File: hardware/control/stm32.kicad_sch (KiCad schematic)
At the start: 18 parts, among them U201 STM32L431RCTx

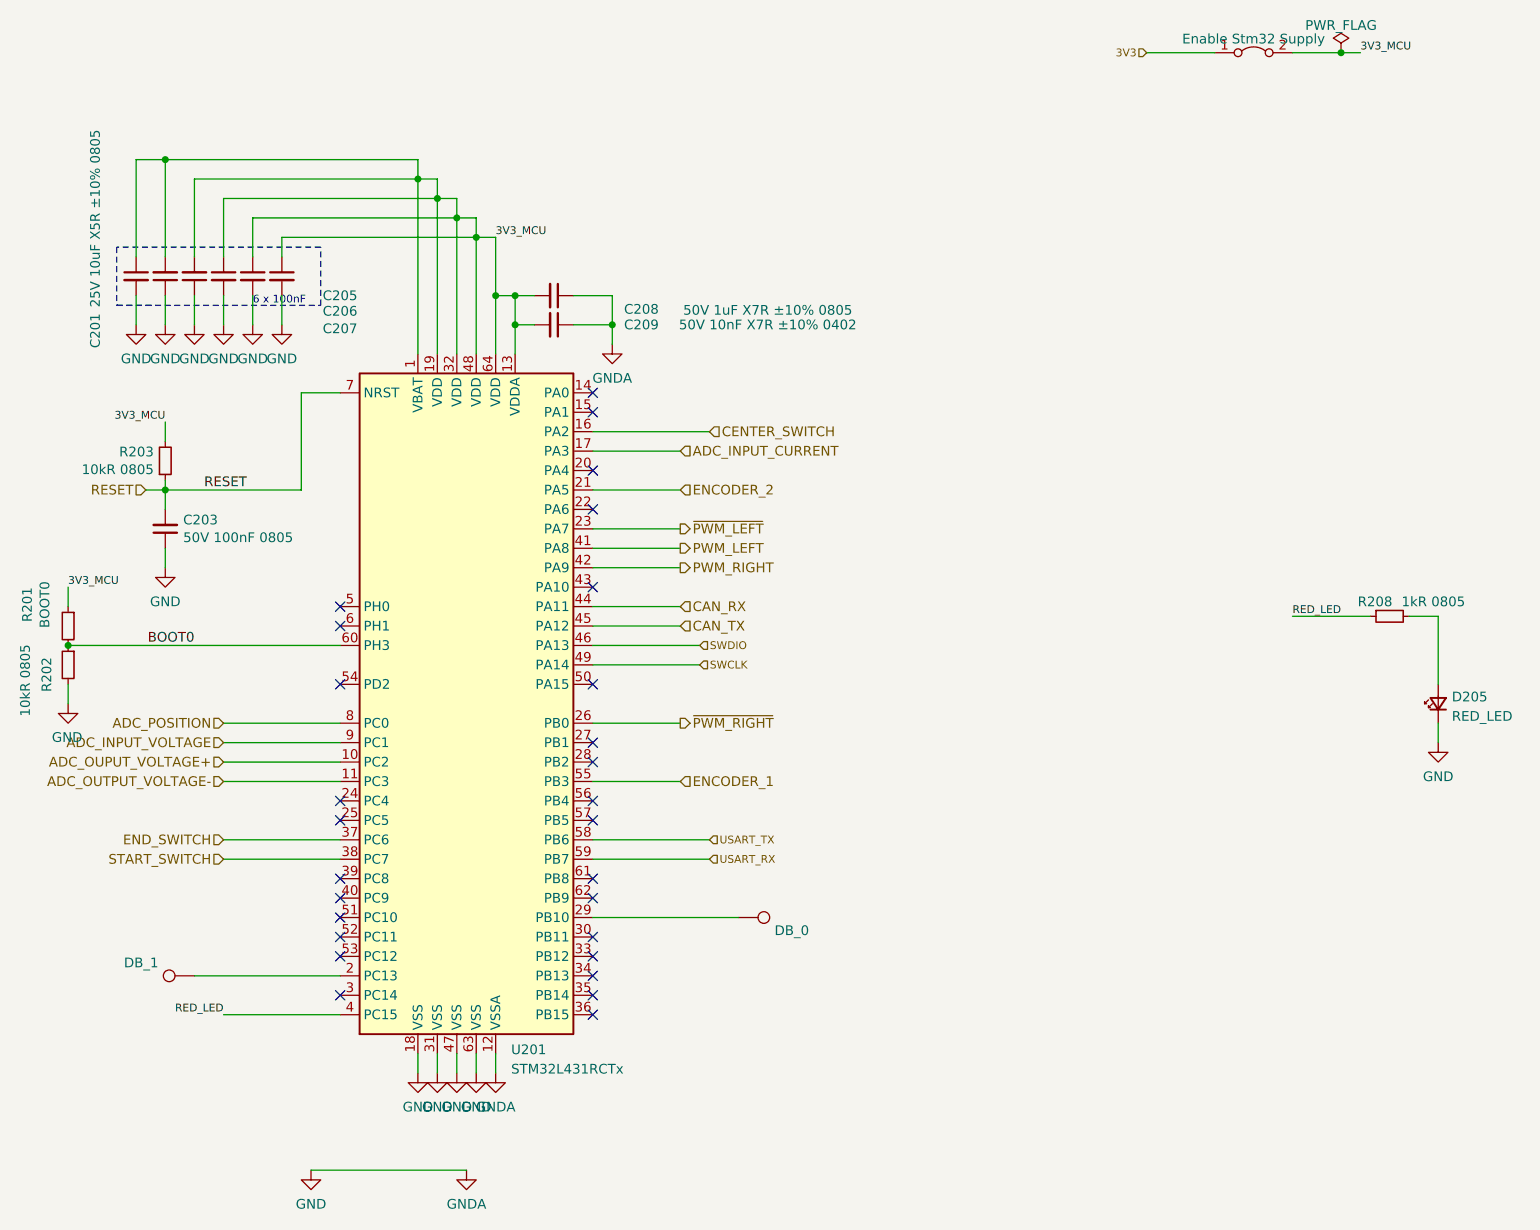
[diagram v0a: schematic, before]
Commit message: Organize schematics per domain
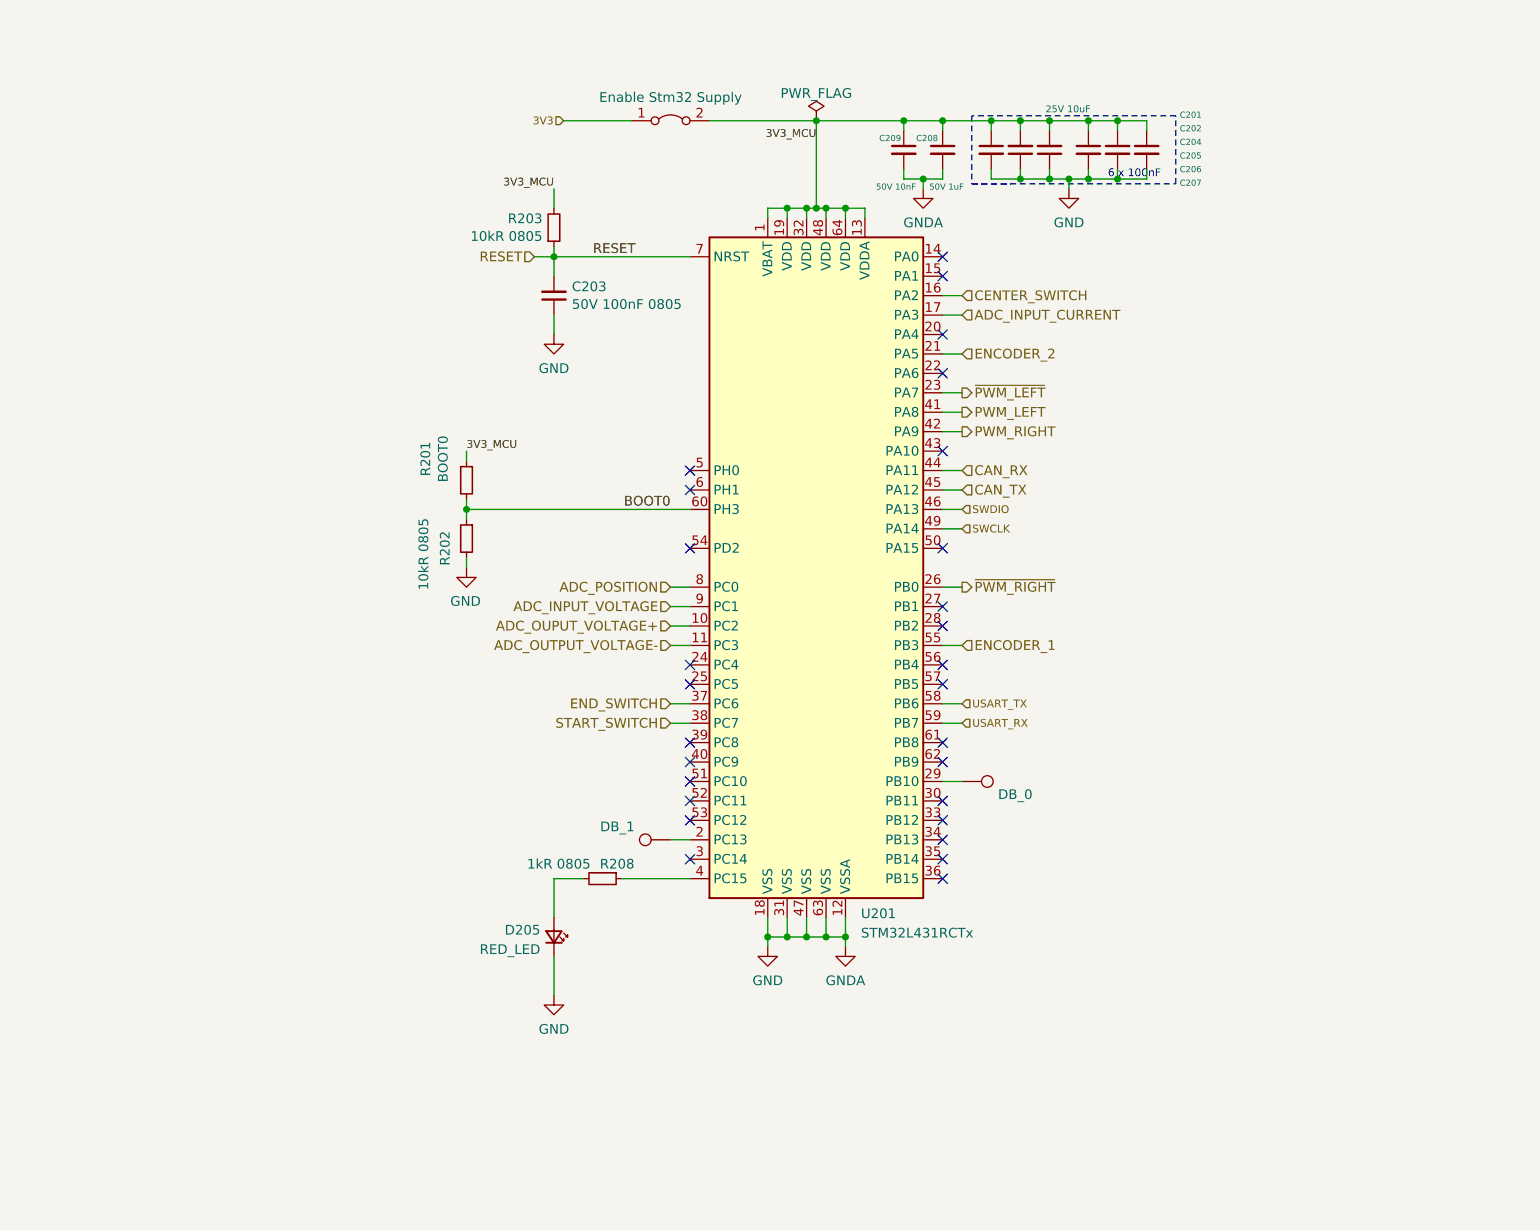
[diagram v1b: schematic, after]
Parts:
- C201: value 25V 10uF X5R ±10% 0805 -> 25V 10uF
- C208: value 50V 1uF X7R ±10% 0805 -> 50V 1uF
- C209: value 50V 10nF X7R ±10% 0402 -> 50V 10nF
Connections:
- net 3V3_MCU: now also C208.1, C209.1; no longer C208.2, C209.2
- net GND: now also C208.2, C209.2; no longer C208.1, C209.1
- net RED_LED: no longer names the net of R208.1, U201.4 (PC15)
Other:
- company: (none) -> Zenite Solar
- title: (none) -> STM32
- moved on the sheet: C201, C203, C205, C206, C207, C208, C209, D205, R201, R202, R203, R208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
